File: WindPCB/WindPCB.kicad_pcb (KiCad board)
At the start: 2 copper layers, 63.5 x 45 mm, 31 parts, among them J6 Conn_01x04, U2 TSR_1-2450, U3 SeeeduinoXIAO, U4 MCP2562-E-P, U5 TSR1-2433E, U6 LM7806_TO220

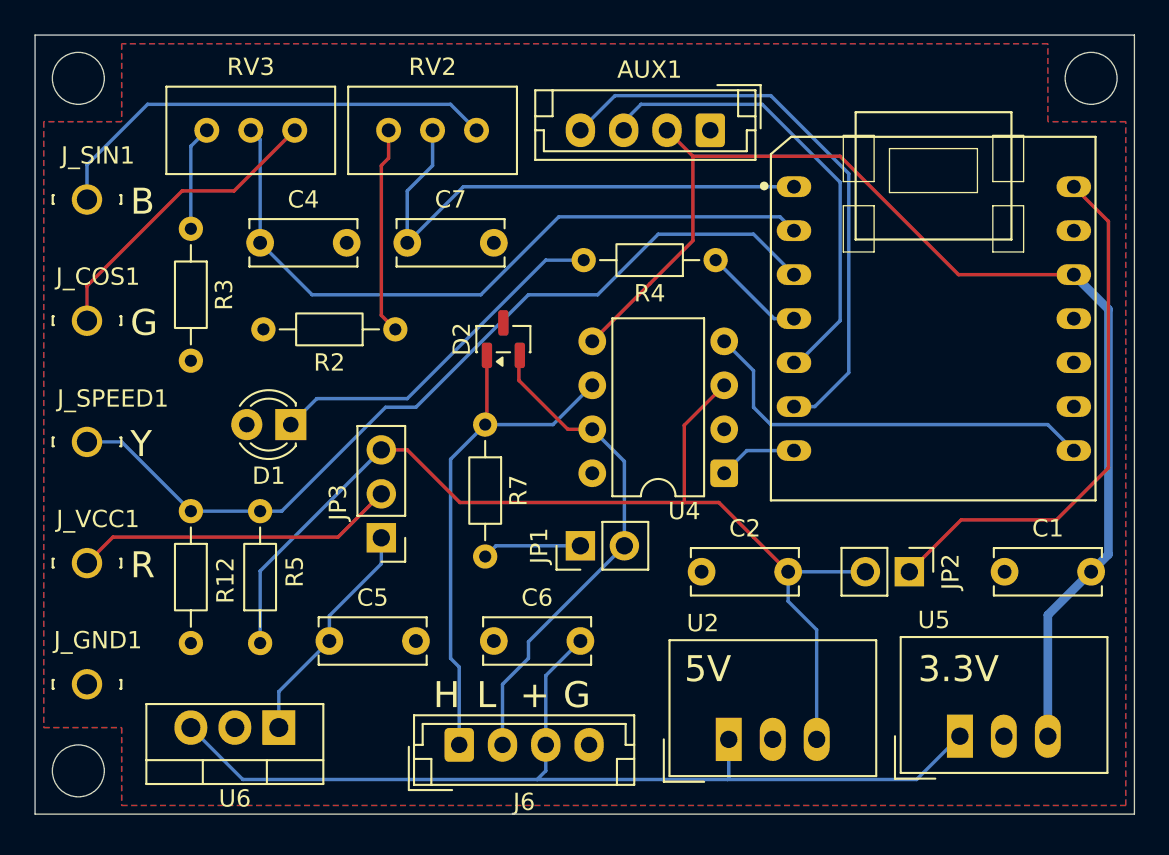
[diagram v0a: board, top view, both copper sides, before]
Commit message: Removed not used code. Dropeed ADS1115 (not advantages). Added suppoer to change teh device name (BLE). Moved N2K info to Constants. Other minor changes and improvements.
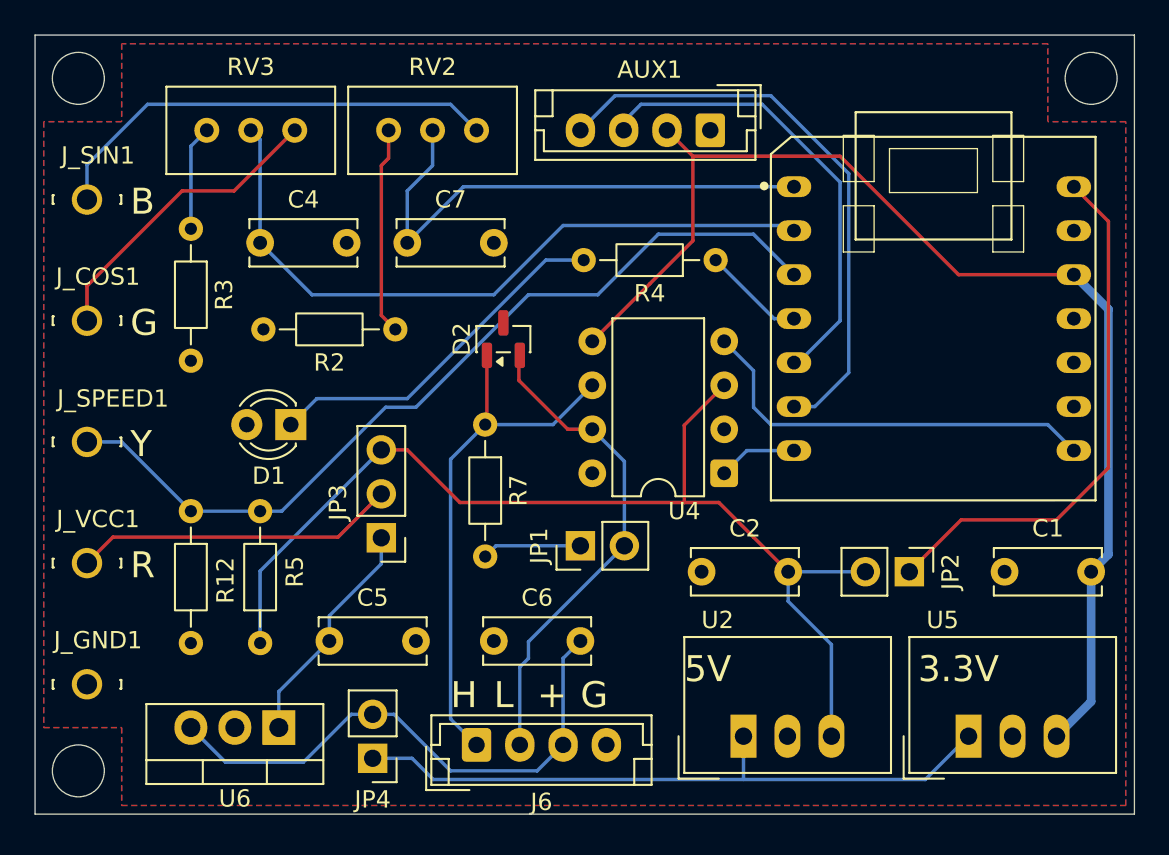
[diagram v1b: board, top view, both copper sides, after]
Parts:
- added JP4: Jumper_2_Open, Connector_PinHeader_2.54mm:PinHeader_1x02_P2.54mm_Vertical, F.Cu at (88.5, 108.3)
- moved J6 1.00 mm to (94.5, 107.5)
- moved U2 0.87 mm to (109.9, 107.0)
- moved U5 0.50 mm to (122.9, 107.0)
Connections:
- U2 pad 1: +12V -> Net-(JP4-A)
- U5 pad 1: +12V -> Net-(JP4-A)
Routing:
- net Net-(JP4-A): track 0.00 -> 38.5 mm
- net +12V: track 58.1 -> 31.9 mm
